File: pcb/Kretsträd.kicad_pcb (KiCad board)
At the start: 2 copper layers, 112.5 x 92.4 mm, 57 parts, among them J1 Conn_01x02_Female, J2 Conn_01x02_Female, SW1 SW_PUSH, SW10 SW_PUSH, SW11 SW_PUSH, SW12 SW_PUSH, SW13 SW_PUSH, SW14 SW_PUSH, SW15 SW_PUSH, SW16 SW_PUSH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

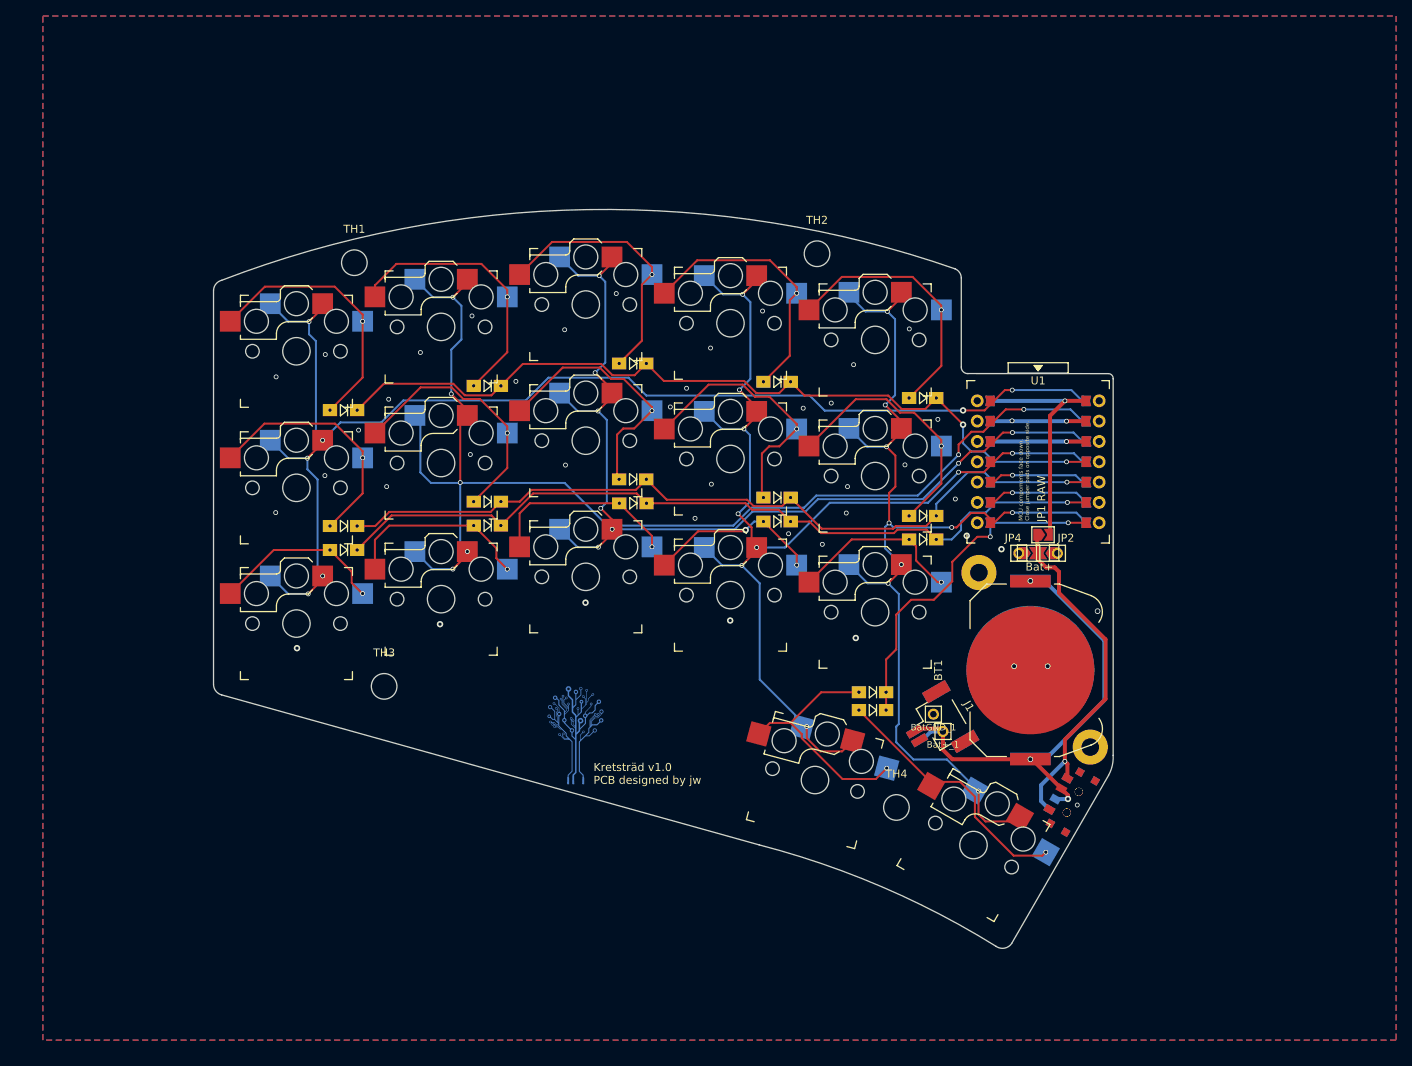
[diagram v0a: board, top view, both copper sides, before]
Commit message: Traces completely re-routed.
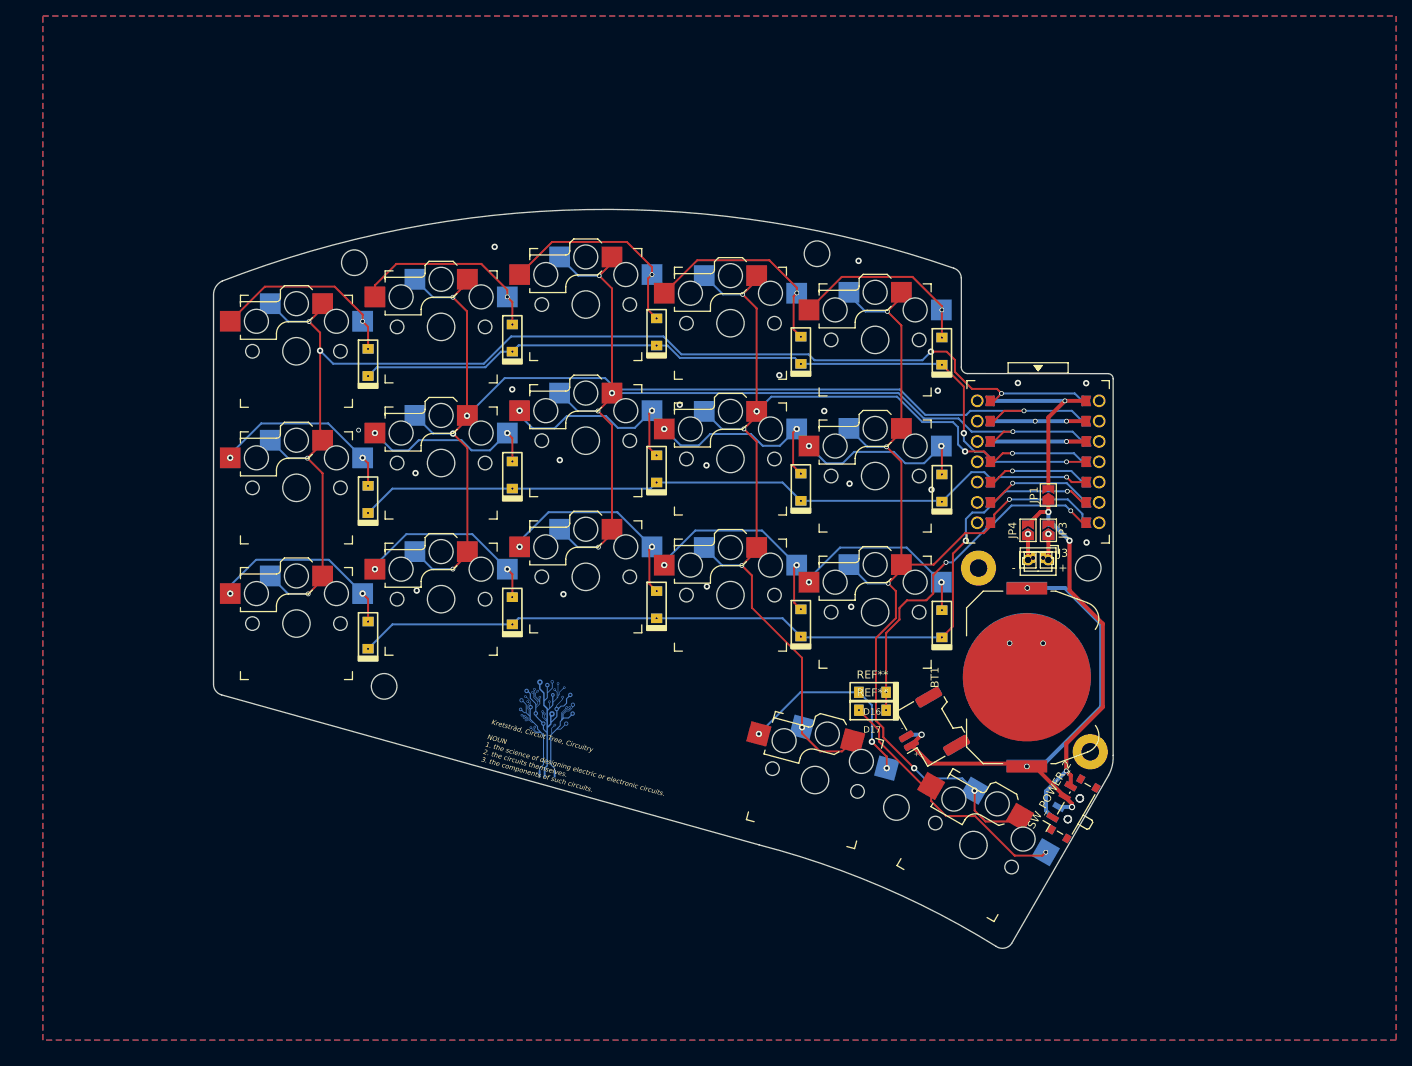
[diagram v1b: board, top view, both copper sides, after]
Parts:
- removed Bat+_1, BatGND_1: MountingHole_Pad, kbd:1pin_conn
- removed the G*** at (127.7, 113.1)
- added G***: circuit_tree_f.cu_12mm, jw_custom_image:circuit_tree_f.cu_12mm, B.Cu at (124.1, 112.2)
- added J3: Conn_01x02_Female, Connector_Molex:Molex_PicoBlade_53047-0210_1x02_P1.25mm_Vertical, F.Cu at (186.1, 90.9)
- added TH5: HOLE, MountingHole:MountingHole_3.2mm_M3, F.Cu at (191.8, 92.2)
- D1, D10, D11, D12, D13, D14, D15, D16, D17, D2, D3, D4, D5, D6, D7, D8, D9: footprint jw_custom:Diode_SOD123_through_hole -> jw_custom_footprint:D_SOD123_THT
- J1, J2: footprint jw_custom_footprint:MOLEX_1x02_1.25mm_51146 -> Connector_Molex:Molex_Panelmate_53780-0270_1x02-1MP_P1.25mm_Horizontal
- JP2: value Hole_2 -> Hole_1; moved to B.Cu
- JP3: value Hole_2 -> Hole_1; moved to F.Cu
- JP4, JP5: value Hole_1 -> Hole_2
- SW_POWER_1, SW_POWER_2: footprint jw_custom_footprint:SPDT_C128955 -> Button_Switch_SMD:SW_SPDT_PCM12
- moved D14 13.0 mm to (155.9, 99.0), turned to 90 degrees
- moved D13 13.0 mm to (137.8, 96.7), turned to 90 degrees
- moved D12 11.1 mm to (119.8, 97.5), turned to 90 degrees
- moved D11 11.1 mm to (101.7, 100.5), turned to 90 degrees
- moved D15 10.8 mm to (173.5, 99.1), turned to 90 degrees
- moved D2 6.74 mm to (119.8, 63.4), turned to 90 degrees
- moved D1 6.71 mm to (101.7, 66.4), turned to 90 degrees
- moved D5 6.34 mm to (173.5, 65.0), turned to 90 degrees
- moved JP1 5.02 mm to (186.8, 83.0), turned to 90 degrees
- moved D3 4.94 mm to (137.8, 62.6), turned to 90 degrees
- moved D4 4.94 mm to (155.9, 64.9), turned to 90 degrees
- moved D7 4.57 mm to (119.8, 80.5), turned to 90 degrees
- moved D6 4.52 mm to (101.7, 83.6), turned to 90 degrees
- moved D10 4.23 mm to (173.5, 82.1), turned to 90 degrees
- moved Hole_1 3.78 mm to (186.8, 91.1), turned to 180 degrees
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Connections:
- Hole_1 pad 1: Net-(Hole_1-Pad1) -> Hole_1
- Hole_2 pad 1: Net-(Hole_2-Pad1) -> Hole_2
- JP2 pad 1: Net-(Hole_2-Pad1) -> Hole_1
- JP3 pad 1: Net-(Hole_2-Pad1) -> Hole_1
- JP4 pad 1: Net-(Hole_1-Pad1) -> Hole_2
- JP5 pad 1: Net-(Hole_1-Pad1) -> Hole_2
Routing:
- net Net-(D5-Pad2): track 32.9 -> 23.7 mm
- net Net-(D10-Pad2): track 32.2 -> 23.1 mm, vias 1 -> 2
- net Net-(D2-Pad2): track 34.2 -> 25.0 mm
- net Net-(D1-Pad2): track 33.4 -> 24.4 mm
- net Net-(D7-Pad2): track 32.1 -> 23.2 mm, vias 1 -> 2
- net Net-(JP1-Pad1): track 44.2 -> 51.4 mm, vias 1 -> 3
- net row2: track 99.8 -> 106.8 mm, vias 1 -> 2
- net Net-(D4-Pad2): track 33.2 -> 26.4 mm
- net Net-(D9-Pad2): track 32.4 -> 25.6 mm, vias 1 -> 2
- net col1: track 148.3 -> 141.5 mm, vias 7 -> 5
- net Net-(D3-Pad2): track 33.3 -> 26.6 mm
- net Net-(D6-Pad2): track 30.8 -> 24.1 mm, vias 1 -> 2
- net row1: track 100.8 -> 94.3 mm
- net Net-(D8-Pad2): track 32.2 -> 26.0 mm, vias 1 -> 2
- net RAW: track 28.4 -> 22.9 mm
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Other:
- outline, holes or cut-outs redrawn
- board text added: "+"
- board text added: "-"
- board text added: "Kretsträd v1 PCB designed by jw"
- board text added: "Kretsträd, Circuit Tree, Circuitry NOUN 1. the science of designing electric or electronic circuits. 2. the circuits themselves. 3. the components of such circuits."
- board text removed: "Bat+"
- board text removed: "GND"
- board text removed: "Kretsträd v1.0 PCB designed by jw"
- board text removed: "MCU compoments face down. Close jumper pads on opposite side."
- board text removed: "RAW"

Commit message: Minor change in front silkscreen text.
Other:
- board text added: "Kretsträd <- Circuit Tree <- Circuitry NOUN 1. the science of designing electric or electronic circuits. 2. the circuits themselves. 3. the components of such circuits."
- board text removed: "Kretsträd, Circuit Tree, Circuitry NOUN 1. the science of designing electric or electronic circuits. 2. the circuits themselves. 3. the components of such circuits."
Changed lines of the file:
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@@
             (xy 0.6582 -1.025)
           ) (width 0) (fill yes))
-    (gr_arc (start 0.55841 -1.01765) (mid 0.004105 -0.877789) (end -0.549888 -1.018884) (width 0.2))
+    (gr_arc (start 0.55841 -1.01765) (mid 0.005117 -0.877788) (end -0.548107 -1.017919) (width 0.2))
       ))
     (pad "1" smd custom (at -5.5118 -7.4478 90) (size 1.3156 0.21) (layers "F.Cu" "F.Mask")
@@
             (xy 0.6582 -1.025)
           ) (width 0) (fill yes))
-    (gr_arc (start 0.55841 -1.01765) (mid 0.004105 -0.877789) (end -0.549888 -1.018884) (width 0.2))
+    (gr_arc (start 0.55841 -1.01765) (mid 0.005117 -0.877788) (end -0.548107 -1.017919) (width 0.2))
       ))
     (pad "2" smd custom (at -5.5118 -4.92 90) (size 1.3156 0.21) (layers "F.Cu" "F.Mask")
@@
             (xy 0.6582 -1.025)
           ) (width 0) (fill yes))
-    (gr_arc (start 0.55841 -1.01765) (mid 0.004105 -0.877789) (end -0.549888 -1.018884) (width 0.2))
+    (gr_arc (start 0.55841 -1.01765) (mid 0.005117 -0.877788) (end -0.548107 -1.017919) (width 0.2))
       ))
     (pad "4" smd custom (at -5.4868 0.16 90) (size 1.3156 0.21) (layers "F.Cu" "F.Mask")
@@
             (xy 0.6582 -1.025)
           ) (width 0) (fill yes))
-    (gr_arc (start 0.55841 -1.01765) (mid 0.004105 -0.877789) (end -0.549888 -1.018884) (width 0.2))
+    (gr_arc (start 0.55841 -1.01765) (mid 0.005117 -0.877788) (end -0.548107 -1.017919) (width 0.2))
       ))
     (pad "5" smd custom (at -5.4868 2.7 90) (size 1.3156 0.21) (layers "F.Cu" "F.Mask")
@@
             (xy 0.6582 -1.025)
           ) (width 0) (fill yes))
-    (gr_arc (start 0.55841 -1.01765) (mid 0.004105 -0.877789) (end -0.549888 -1.018884) (width 0.2))
+    (gr_arc (start 0.55841 -1.01765) (mid 0.005117 -0.877788) (end -0.548107 -1.017919) (width 0.2))
       ))
     (pad "6" smd custom (at -5.4868 5.24 90) (size 1.3156 0.21) (layers "F.Cu" "F.Mask")
@@
             (xy 0.6582 -1.025)
           ) (width 0) (fill yes))
-    (gr_arc (start 0.55841 -1.01765) (mid 0.004105 -0.877789) (end -0.549888 -1.018884) (width 0.2))
+    (gr_arc (start 0.55841 -1.01765) (mid 0.005117 -0.877788) (end -0.548107 -1.017919) (width 0.2))
       ))
     (pad "7" smd custom (at -5.4868 7.78 90) (size 1.3156 0.21) (layers "F.Cu" "F.Mask")
@@
             (xy 0.6582 -1.025)
           ) (width 0) (fill yes))
-    (gr_arc (start 0.55841 -1.01765) (mid 0.004105 -0.877789) (end -0.549888 -1.018884) (width 0.2))
+    (gr_arc (start 0.55841 -1.01765) (mid 0.005117 -0.877788) (end -0.548107 -1.017919) (width 0.2))
       ))
     (pad "8" smd custom (at 5.5398 7.78 270) (size 1.3156 0.21) (layers "F.Cu" "F.Mask")
@@
             (xy 0.6582 -1.025)
           ) (width 0) (fill yes))
-    (gr_arc (start 0.55841 -1.01765) (mid 0.004105 -0.877789) (end -0.549888 -1.018884) (width 0.2))
+    (gr_arc (start 0.55841 -1.01765) (mid 0.005117 -0.877788) (end -0.548107 -1.017919) (width 0.2))
       ))
     (pad "9" smd custom (at -5.4868 5.24 90) (size 1.3156 0.21) (layers "B.Cu" "B.Mask")
@@
             (xy 0.6582 -1.025)
           ) (width 0) (fill yes))
-    (gr_arc (start 0.55841 -1.01765) (mid 0.004105 -0.877789) (end -0.549888 -1.018884) (width 0.2))
+    (gr_arc (start 0.55841 -1.01765) (mid 0.005117 -0.877788) (end -0.548107 -1.017919) (width 0.2))
       ))
     (pad "9" smd custom (at 5.5398 5.24 270) (size 1.3156 0.21) (layers "F.Cu" "F.Mask")
@@
             (xy 0.6582 -1.025)
           ) (width 0) (fill yes))
-    (gr_arc (start 0.55841 -1.01765) (mid 0.004105 -0.877789) (end -0.549888 -1.018884) (width 0.2))
+    (gr_arc (start 0.55841 -1.01765) (mid 0.005117 -0.877788) (end -0.548107 -1.017919) (width 0.2))
       ))
     (pad "11" smd custom (at -5.4868 0.16 90) (size 1.3156 0.21) (layers "B.Cu" "B.Mask")
@@
             (xy 0.6582 -1.025)
           ) (width 0) (fill yes))
-    (gr_arc (start 0.55841 -1.01765) (mid 0.004105 -0.877789) (end -0.549888 -1.018884) (width 0.2))
+    (gr_arc (start 0.55841 -1.01765) (mid 0.005117 -0.877788) (end -0.548107 -1.017919) (width 0.2))
       ))
     (pad "11" smd custom (at 5.5398 0.16 270) (size 1.3156 0.21) (layers "F.Cu" "F.Mask")
@@
             (xy 0.6582 -1.025)
           ) (width 0) (fill yes))
-    (gr_arc (start 0.55841 -1.01765) (mid 0.004105 -0.877789) (end -0.549888 -1.018884) (width 0.2))
+    (gr_arc (start 0.55841 -1.01765) (mid 0.005117 -0.877788) (end -0.548107 -1.017919) (width 0.2))
       ))
     (pad "12" smd custom (at 5.5398 -2.38 270) (size 1.3156 0.21) (layers "F.Cu" "F.Mask")
@@
             (xy 0.6582 -1.025)
           ) (width 0) (fill yes))
-    (gr_arc (start 0.55841 -1.01765) (mid 0.004105 -0.877789) (end -0.549888 -1.018884) (width 0.2))
+    (gr_arc (start 0.55841 -1.01765) (mid 0.005117 -0.877788) (end -0.548107 -1.017919) (width 0.2))
       ))
     (pad "14" smd custom (at 5.5118 -7.4478 270) (size 1.3156 0.21) (layers "F.Cu" "F.Mask")
@@
             (xy 0.6582 -1.025)
           ) (width 0) (fill yes))
-    (gr_arc (start 0.55841 -1.01765) (mid 0.004105 -0.877789) (end -0.549888 -1.018884) (width 0.2))
+    (gr_arc (start 0.55841 -1.01765) (mid 0.005117 -0.877788) (end -0.548107 -1.017919) (width 0.2))
       ))
   )
@@
     (fp_line (start -2.5 2.2) (end -2.5 1.5) (layer "B.SilkS") (width 0.15))
     (fp_arc (start -2.5 6.2) (mid -2.146447 6.346447) (end -2 6.7) (layer "B.SilkS") (width 0.15))
-    (fp_arc (start -1 3.7) (mid -2.06066 3.260659) (end -2.5 2.2) (layer "B.SilkS") (width 0.15))
+    (fp_arc (start -1 3.7) (mid -2.06066 3.26066) (end -2.5 2.2) (layer "B.SilkS") (width 0.15))
     (fp_line (start -7 -6) (end -7 -7) (layer "F.SilkS") (width 0.15))
     (fp_line (start 2.5 1.5) (end 7 1.5) (layer "F.SilkS") (width 0.15))
@@
     (fp_line (start 2 4.25) (end 2 7.7) (layer "B.Fab") (width 0.12))
     (fp_arc (start -2.5 6.2) (mid -2.146447 6.346447) (end -2 6.7) (layer "B.Fab") (width 0.15))
-    (fp_arc (start -1 3.7) (mid -2.06066 3.260659) (end -2.5 2.2) (layer "B.Fab") (width 0.15))
+    (fp_arc (start -1 3.7) (mid -2.06066 3.26066) (end -2.5 2.2) (layer "B.Fab") (width 0.15))
     (fp_line (start -1.5 3.7) (end 1 3.7) (layer "F.Fab") (width 0.15))
     (fp_line (start -1.5 8.2) (end 1.5 8.2) (layer "F.Fab") (width 0.15))
@@
     (effects (font (size 0.6 0.6) (thickness 0.15)) (justify left))
   )
-  (gr_text "Kretsträd, Circuit Tree, Circuitry\n\nNOUN\n1. the science of designing electric or electronic circuits.\n2. the circuits themselves.\n3. the components of such circuits." (at 116.531758 113.691391 -15.5) (layer "F.SilkS")
+  (gr_text "Kretsträd <- Circuit Tree <- Circuitry\n\nNOUN\n1. the science of designing electric or electronic circuits.\n2. the circuits themselves.\n3. the components of such circuits." (at 116.531758 113.691391 -15.5) (layer "F.SilkS")
     (effects (font (size 0.6 0.6) (thickness 0.12) italic) (justify left))
   )

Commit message: Tones of changes.
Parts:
- removed the G*** at (124.1, 112.2)
- removed SW_POWER_1, SW_POWER_2: SW_SPDT, Button_Switch_SMD:SW_SPDT_PCM12
- added G***: circuit_tree_f.cu_3_10mm, jw_custom_image:circuit_tree_f.cu_3_10mm, B.Cu at (109.9, 111.4)
- added JP6: Hole_2, Jumper:SolderJumper-2_P1.3mm_Open_RoundedPad1.0x1.5mm, B.Cu at (182.9, 87.5)
- added PWR_SW_1: SW_SPDT, Button_Switch_SMD:SW_SPDT_PCM12, F.Cu at (190.3, 123.0)
- added PWR_SW_2: SW_SPDT, Button_Switch_SMD:SW_SPDT_PCM12, B.Cu at (190.3, 123.0)
- D1, D10, D11, D12, D13, D14, D15, D16, D17, D2, D3, D4, D5, D6, D7, D8, D9: footprint jw_custom_footprint:D_SOD123_THT -> jw_custom_footprint:Diode_SOD123_THT_2
- JP1, JP3: footprint Jumper:SolderJumper-2_P1.3mm_Open_TrianglePad1.0x1.5mm -> Jumper:SolderJumper-2_P1.3mm_Open_RoundedPad1.0x1.5mm
- JP2: value Hole_1 -> to_RAW; footprint Jumper:SolderJumper-2_P1.3mm_Open_TrianglePad1.0x1.5mm -> Jumper:SolderJumper-2_P1.3mm_Open_RoundedPad1.0x1.5mm
- JP4: value Hole_2 -> Hole_1; footprint Jumper:SolderJumper-2_P1.3mm_Open_TrianglePad1.0x1.5mm -> Jumper:SolderJumper-2_P1.3mm_Open_RoundedPad1.0x1.5mm; moved to B.Cu
- JP5: footprint Jumper:SolderJumper-2_P1.3mm_Open_TrianglePad1.0x1.5mm -> Jumper:SolderJumper-2_P1.3mm_Open_RoundedPad1.0x1.5mm; moved to F.Cu
- moved JP1 4.81 mm to (188.4, 87.5)
- moved J1 1.96 mm to (171.8, 114.3)
- moved J2 1.96 mm to (171.8, 114.3)
- moved SW16 1.96 mm to (157.6, 120.6)
- moved SW17 1.96 mm to (177.4, 128.7)
- moved TH4 1.96 mm to (167.8, 124.0)
- moved JP2 1.61 mm to (188.4, 87.5)
- moved JP5 1.39 mm to (182.9, 87.5)
- moved JP3 1.37 mm to (185.4, 87.5)
- moved D17 1.30 mm to (164.3, 111.1)
- moved JP4 1.19 mm to (185.4, 87.6)
- moved D16 0.89 mm to (164.3, 108.4)
- moved TH_PCB_2 0.74 mm to (192.0, 115.8)
- moved D13 0.51 mm to (137.8, 96.2)
- moved D3 0.51 mm to (137.8, 62.1)
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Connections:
- JP2 pad 1: Hole_1 -> Net-(JP1-Pad1)
- JP2 pad 2: Net-(JP1-Pad1) -> RAW
- JP4 pad 1: Hole_2 -> Hole_1
- JP5 pad 2: GND -> Net-(JP1-Pad1)
- SW1 pad : (no net) -> col0
- SW11 pad : (no net) -> col0
- SW6 pad : (no net) -> col0
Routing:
- net RAW: track 22.9 -> 27.4 mm, vias 1 -> 2
- net BT+: track 59.2 -> 62.4 mm
- net SCL: track 13.3 -> 11.3 mm
- net row1: track 94.3 -> 92.5 mm
- net Net-(D16-Pad2): track 25.6 -> 27.0 mm
- net Net-(JP1-Pad1): track 51.4 -> 50.1 mm
- net VCC: track 11.1 -> 9.86 mm
- net SDA: track 12.2 -> 11.0 mm
- net GND: track 11.0 -> 9.88 mm, vias 24 -> 26
- net Net-(D17-Pad2): track 31.8 -> 32.8 mm
- net col4: track 126.5 -> 127.4 mm
- net col1: track 141.5 -> 140.7 mm
- net Net-(D2-Pad2): track 25.0 -> 24.3 mm, vias 1 -> 2
- net row0: track 100.7 -> 101.4 mm
- net row2: track 106.8 -> 106.2 mm
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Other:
- board size 112.5 x 92.4 mm -> 112.5 x 95.1 mm
- board text added: "Kretsträd PCB designed by jw"
- board text added: "L:112.5 H:95.1"
- board text removed: "Kretsträd v1 PCB designed by jw"
